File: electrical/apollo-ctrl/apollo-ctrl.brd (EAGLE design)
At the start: 100 x 80 mm, 61 parts, among them Q1 N-chan, Q2 N-chan, U1 NANO, U2 ADAFRUIT-MPRLS, X1 BARREL-JACK, X2 SENSOR-O2

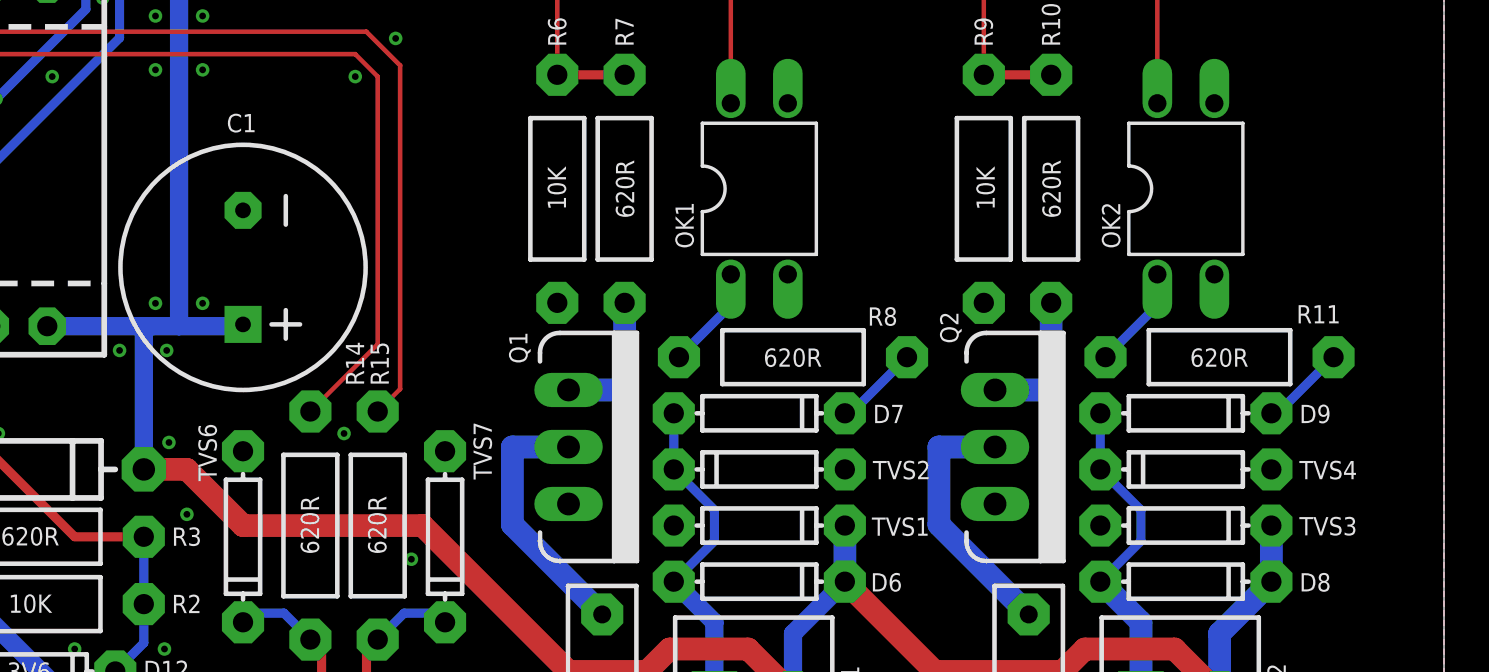
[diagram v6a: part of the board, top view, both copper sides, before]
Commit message: added a fan header
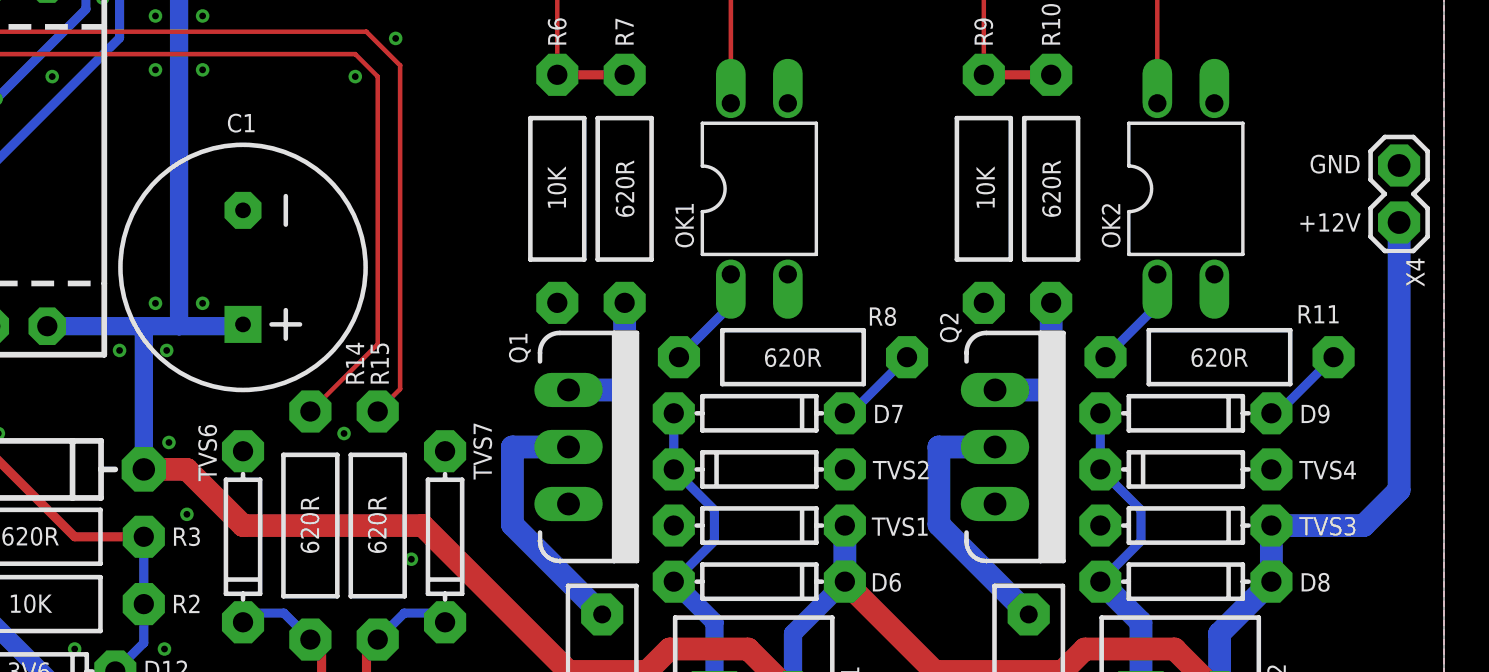
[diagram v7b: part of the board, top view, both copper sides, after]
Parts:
- added X4: FAN, apollo-ctrl:1X02
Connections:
- net +12V: now also X4.1
- net GND: now also X4.2
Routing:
- net +12V: track 110.1 -> 128.4 mm
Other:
- board text added: "+12V"
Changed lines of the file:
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@@
 <text x="37.8" y="76.6" size="0.8128" layer="21" font="vector" ratio="12" rot="R270" align="center-left">GND</text>
 <text x="17.6" y="53" size="0.8128" layer="21" font="vector" ratio="12" rot="R270" align="center-left">VIN</text>
+<text x="96.3" y="27.6" size="0.8128" layer="21" font="vector" ratio="12" align="center-right">GND</text>
+<text x="96.3" y="25" size="0.8128" layer="21" font="vector" ratio="12" align="center-right">+12V</text>
 </plain>
 <attributes>
@@
 <attribute name="VALUE" x="8.189" y="23.392" size="0.4064" layer="28" rot="MR90"/>
 </element>
+<element name="X4" library="apollo-ctrl" package="1X02" value="FAN" x="98" y="25" smashed="yes" rot="R90">
+<attribute name="NAME" x="98.7288" y="23.4462" size="0.8128" layer="25" font="vector" ratio="10" rot="R270" align="center-left"/>
+<attribute name="VALUE" x="97.625" y="23.37" size="0.8128" layer="27" font="vector" rot="R270" align="center-left"/>
+</element>
 </elements>
 <signals>
@@
 <via x="20" y="52" extent="1-16" drill="0.3" shape="octagon"/>
 <via x="19.3" y="50.45" extent="1-16" drill="0.3" shape="octagon"/>
+<contactref element="X4" pad="2"/>
 </signal>
 <signal name="COIL-1-CHECK">
@@
 <contactref element="D6" pad="C"/>
 <contactref element="TVS1" pad="C"/>
-<wire x1="42.5" y1="20.38" x2="42.08" y2="20.38" width="0.8128" layer="16"/>
 <wire x1="71" y1="4" x2="71" y2="6.69" width="0.8128" layer="16"/>
 <wire x1="71" y1="6.69" x2="73.31" y2="9" width="0.8128" layer="16"/>
@@
 <wire x1="44" y1="14" x2="42.08" y2="14" width="1.016" layer="1"/>
 <wire x1="43.65" y1="45" x2="43.65" y2="20.38" width="0.8128" layer="16"/>
-<wire x1="43.65" y1="20.38" x2="42.5" y2="20.38" width="0.8128" layer="16"/>
+<wire x1="43.65" y1="20.38" x2="42.08" y2="20.38" width="0.8128" layer="16"/>
+<contactref element="X4" pad="1"/>
+<wire x1="92.31" y1="11.5" x2="96.4188625" y2="11.5" width="1.016" layer="16"/>
+<wire x1="96.4188625" y1="11.5" x2="98" y2="13.0811375" width="1.016" layer="16"/>
+<wire x1="98" y1="13.0811375" x2="98" y2="25" width="1.016" layer="16"/>
 </signal>
 <signal name="N$14">

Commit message: minor tweaks for ctrl pcb before fab
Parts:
- added SG2, SG3, SG4: BUZZER, apollo-ctrl:1X01NS
- D2, D4, D5: value (none) -> DIODE-SCHOTTKYPTH
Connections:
- net BUZZ: now also SG2.1, SG3.1, SG4.1
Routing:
- net BUZZ: track 98.1 -> 109.6 mm
- net N$6: track 9.41 -> 12.1 mm
